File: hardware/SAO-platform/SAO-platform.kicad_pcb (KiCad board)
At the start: 2 copper layers, 85 parts, among them U1 WCH CH32V003F4U6

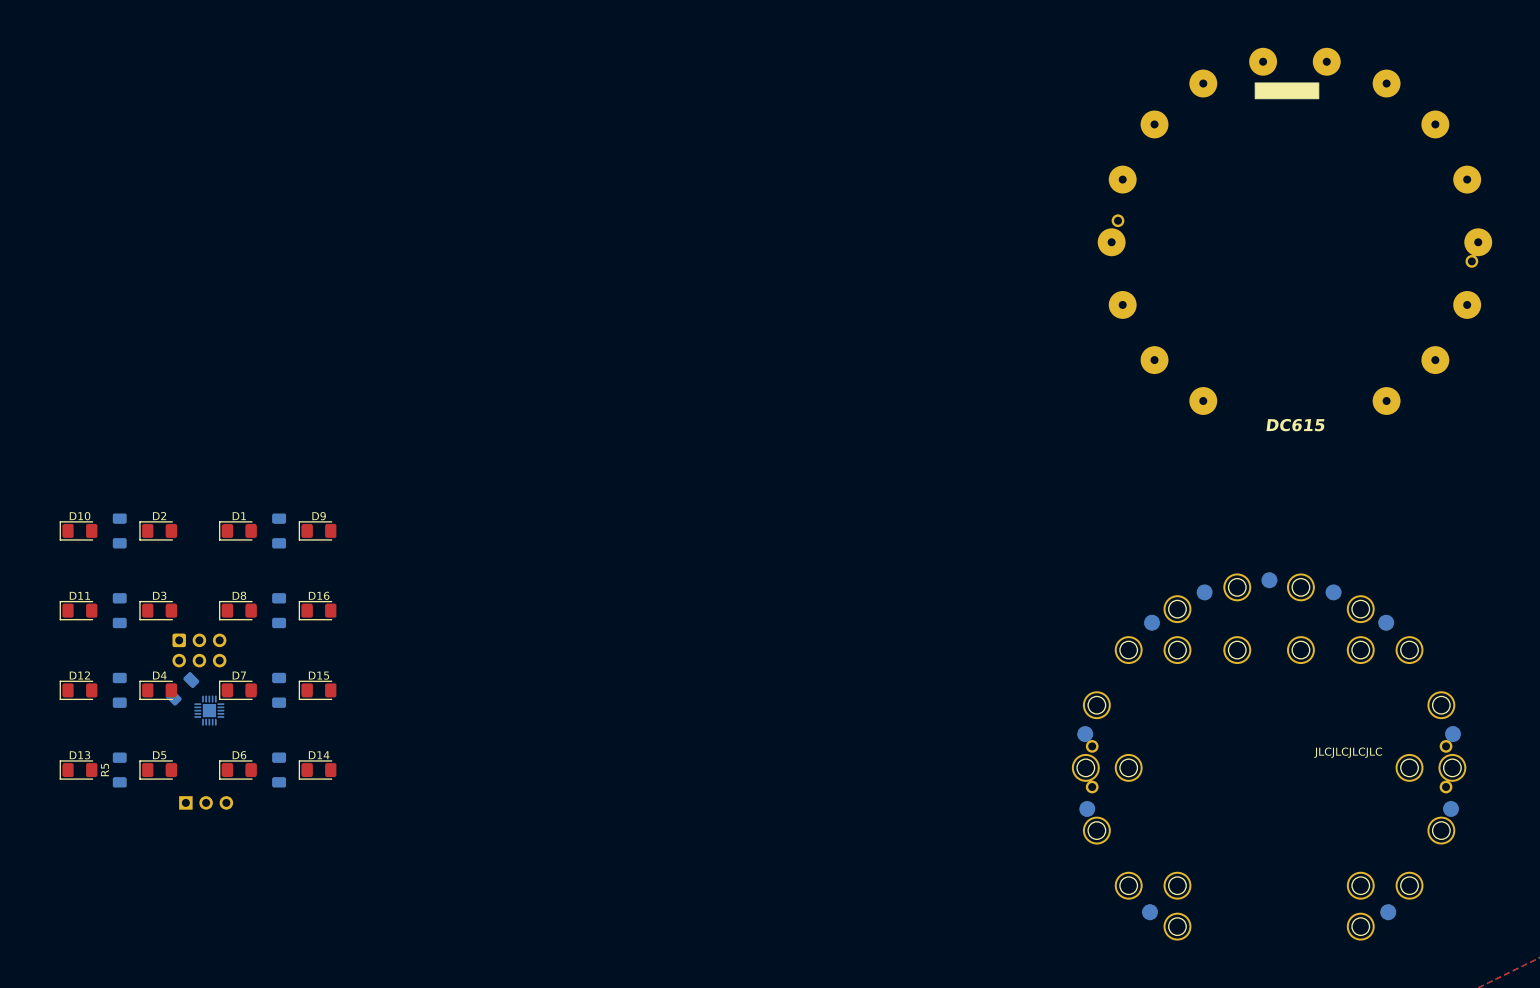
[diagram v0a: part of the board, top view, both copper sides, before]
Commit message: layout complete, passes DRC
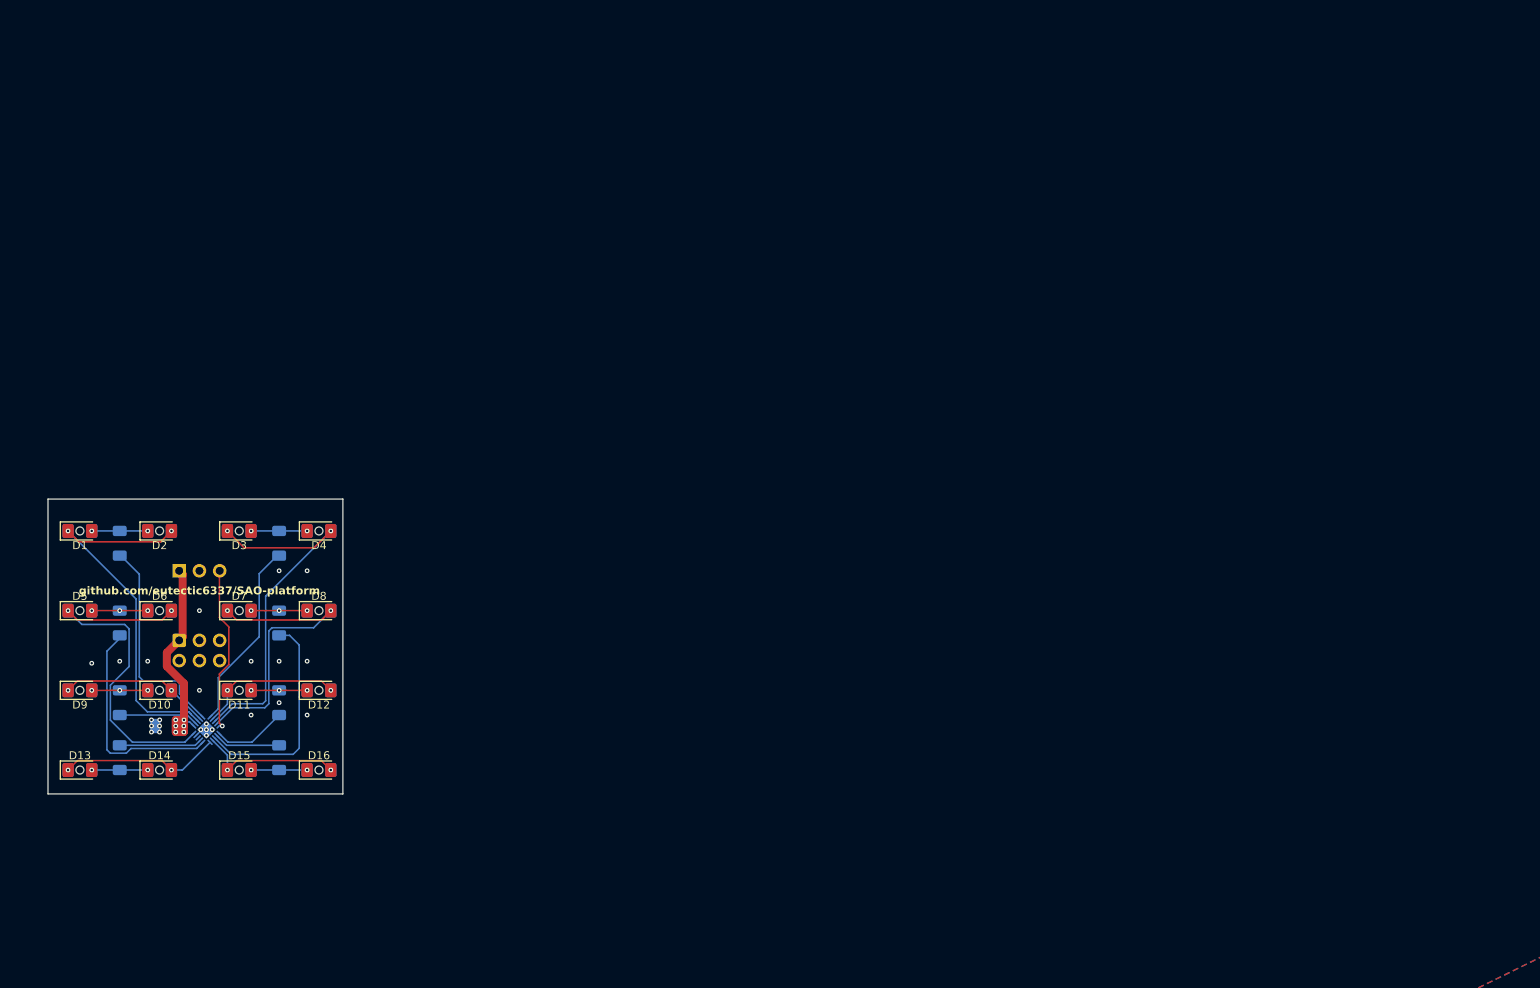
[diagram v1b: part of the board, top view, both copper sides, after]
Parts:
- removed align-io1, align-io2, align-ir1, align-ir2, align-o1, align-o2: , 
- removed aperture-D1, aperture-D10, aperture-D11, aperture-D12, aperture-D13, aperture-D14, aperture-D15, aperture-D16, aperture-D2, aperture-D3, aperture-D4, aperture-D5, aperture-D6, aperture-D7, aperture-D8, aperture-D9: TestPoint_THTPad_D1.0mm_Drill0.5mm, TestPoint:TestPoint_THTPad_D1.0mm_Drill0.5mm
- removed clearance-D1, clearance-D10, clearance-D11, clearance-D12, clearance-D13, clearance-D14, clearance-D15, clearance-D16, clearance-D2, clearance-D3, clearance-D4, clearance-D5, clearance-D6, clearance-D7, clearance-D8, clearance-D9, clearance-R1, clearance-R2, clearance-R3, clearance-R4, clearance-R5, clearance-R6, clearance-R7, clearance-R8: TestPoint_THTPad_3.0x3.0mm_Drill1.5mm, TestPoint:TestPoint_THTPad_3.0x3.0mm_Drill1.5mm
- removed stitch2 (x11): TestPoint_Pad_D2.0mm, TestPoint:TestPoint_Pad_D2.0mm
- added h1: , , F.Cu at (105.0, 85.0)
- added h10: , , F.Cu at (85.0, 85.0)
- added h11: , , F.Cu at (85.0, 95.0)
- added h12: , , F.Cu at (85.0, 105.0)
- added h13: , , F.Cu at (85.0, 115.0)
- added h14: , , F.Cu at (115.0, 115.0)
- added h15: , , F.Cu at (115.0, 105.0)
- added h16: , , F.Cu at (115.0, 95.0)
- added h2: , , F.Cu at (95.0, 85.0)
- added h3: , , F.Cu at (95.0, 95.0)
- added h4: , , F.Cu at (95.0, 105.0)
- added h5: , , F.Cu at (95.0, 115.0)
- added h6: , , F.Cu at (105.0, 115.0)
- added h7: , , F.Cu at (105.0, 105.0)
- added h8: , , F.Cu at (105.0, 95.0)
- added h9: , , F.Cu at (115.0, 85.0)
- added rD1: LED, LED_SMD:LED_1206_3216Metric_Pad1.42x1.75mm_HandSolder, B.Cu at (85.0, 85.0)
- added rD10: LED, LED_SMD:LED_1206_3216Metric_Pad1.42x1.75mm_HandSolder, B.Cu at (95.0, 105.0)
- added rD11: LED, LED_SMD:LED_1206_3216Metric_Pad1.42x1.75mm_HandSolder, B.Cu at (105.0, 105.0)
- added rD12: LED, LED_SMD:LED_1206_3216Metric_Pad1.42x1.75mm_HandSolder, B.Cu at (115.0, 105.0)
- added rD13: LED, LED_SMD:LED_1206_3216Metric_Pad1.42x1.75mm_HandSolder, B.Cu at (85.0, 115.0)
- added rD14: LED, LED_SMD:LED_1206_3216Metric_Pad1.42x1.75mm_HandSolder, B.Cu at (95.0, 115.0)
- added rD15: LED, LED_SMD:LED_1206_3216Metric_Pad1.42x1.75mm_HandSolder, B.Cu at (105.0, 115.0)
- added rD16: LED, LED_SMD:LED_1206_3216Metric_Pad1.42x1.75mm_HandSolder, B.Cu at (115.0, 115.0)
- added rD2: LED, LED_SMD:LED_1206_3216Metric_Pad1.42x1.75mm_HandSolder, B.Cu at (95.0, 85.0)
- added rD3: LED, LED_SMD:LED_1206_3216Metric_Pad1.42x1.75mm_HandSolder, B.Cu at (105.0, 85.0)
- added rD4: LED, LED_SMD:LED_1206_3216Metric_Pad1.42x1.75mm_HandSolder, B.Cu at (115.0, 85.0)
- added rD5: LED, LED_SMD:LED_1206_3216Metric_Pad1.42x1.75mm_HandSolder, B.Cu at (85.0, 95.0)
- added rD6: LED, LED_SMD:LED_1206_3216Metric_Pad1.42x1.75mm_HandSolder, B.Cu at (95.0, 95.0)
- added rD7: LED, LED_SMD:LED_1206_3216Metric_Pad1.42x1.75mm_HandSolder, B.Cu at (105.0, 95.0)
- added rD8: LED, LED_SMD:LED_1206_3216Metric_Pad1.42x1.75mm_HandSolder, B.Cu at (115.0, 95.0)
- added rD9: LED, LED_SMD:LED_1206_3216Metric_Pad1.42x1.75mm_HandSolder, B.Cu at (85.0, 105.0)
- moved PROG1 29.1 mm to (97.5, 90.0)
- moved C1 5.02 mm to (96.0, 109.5), turned to 180 degrees
- moved U1 2.42 mm to (100.9, 109.9), turned to 45 degrees
- moved R1 1.55 mm to (90.0, 86.6)
- moved R2 1.55 mm to (110.0, 86.6)
- moved R3 1.55 mm to (90.0, 96.6)
- moved R4 1.55 mm to (110.0, 96.6)
- moved R5 1.55 mm to (90.0, 106.6), turned to 90 degrees
- moved R6 1.55 mm to (110.0, 106.6), turned to 90 degrees
- moved R7 1.55 mm to (90.0, 113.4)
- moved R8 1.55 mm to (110.0, 113.4)
- renumbered D10 to D1, D4 to D10, D7 to D11, D15 to D12, D5 to D14, D6 to D15, D14 to D16, D1 to D3, D9 to D4, D11 to D5, D3 to D6, D8 to D7, D16 to D8, D12 to D9, R2 to R1, R1 to R2, R8 to R4, R4 to R5, R7 to R6, R5 to R7, R6 to R8
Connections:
- D1 pad 1: Net-(D10-K) -> GP1
- D1 pad 2: GP2 -> Net-(D1-A)
- D10 pad 1: GP4 -> Net-(D10-K)
- D10 pad 2: Net-(D12-K) -> GP5
- D11 pad 1: GP7 -> GP6
- D12 pad 2: GP7 -> GP6
- D13 pad 1: Net-(D13-K) -> GP7
- D13 pad 2: GP5 -> Net-(D13-A)
- D14 pad 1: GP5 -> Net-(D13-A)
- D14 pad 2: Net-(D13-K) -> GP7
- D15 pad 1: GP6 -> GP8
- D16 pad 2: GP6 -> GP8
- D2 pad 1: GP2 -> Net-(D1-A)
- D2 pad 2: Net-(D10-K) -> GP1
- D3 pad 1: GP1 -> GP2
- D4 pad 2: GP1 -> GP2
- D5 pad 1: Net-(D11-K) -> GP3
- D5 pad 2: GP3 -> Net-(D5-A)
- D6 pad 1: GP3 -> Net-(D5-A)
- D6 pad 2: Net-(D11-K) -> GP3
- D7 pad 1: GP8 -> GP4
- D8 pad 2: GP8 -> GP4
- D9 pad 1: Net-(D12-K) -> GP5
- D9 pad 2: GP4 -> Net-(D10-K)
- R1 pad 1: PWM2 -> PWM1
- R1 pad 2: Net-(D10-K) -> Net-(D1-A)
- R2 pad 1: PWM1 -> PWM2
- R3 pad 2: Net-(D11-K) -> Net-(D5-A)
- R4 pad 1: PWM8 -> PWM4
- R5 pad 1: PWM4 -> PWM5
- R5 pad 2: Net-(D12-K) -> Net-(D10-K)
- R6 pad 1: PWM7 -> PWM6
- R7 pad 1: PWM5 -> PWM7
- R7 pad 2: Net-(D13-K) -> Net-(D13-A)
- R8 pad 1: PWM6 -> PWM8
- U1 pad 1: PWM4 -> PWM3
- U1 pad 11: PWM8 -> PWM2
- U1 pad 12: GP8 -> GP6
- U1 pad 13: GP6 -> GP2
- U1 pad 14: GP7 -> GP4
- U1 pad 16: PWM7 -> PWM6
- U1 pad 17: PWM6 -> PWM8
- U1 pad 18: PWM5 -> PWM4
- U1 pad 19: GP5 -> GP8
- U1 pad 2: PWM3 -> PWM7
- U1 pad 20: GP4 -> GP7
- U1 pad 7: PWM2 -> PWM5
- U1 pad 8: GP2 -> GP1
- U1 pad 9: GP1 -> GP5
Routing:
- net GP1: track 0.00 -> 48.3 mm, vias 0 -> 2
- net GP3: track 0.00 -> 47.0 mm, vias 0 -> 2
- net GP2: track 0.00 -> 46.9 mm, vias 0 -> 2
- net GP4: track 0.00 -> 39.5 mm, vias 0 -> 2
- net +3V0: track 0.00 -> 28.1 mm, vias 0 -> 6
- net PWM4: track 0.00 -> 27.8 mm
- net PWM3: track 0.00 -> 27.8 mm
- net PWM1: track 0.00 -> 27.1 mm
- net PWM2: track 0.00 -> 24.0 mm
- net /SWIO: track 0.00 -> 20.6 mm, vias 0 -> 1
- net GP7: track 0.00 -> 20.2 mm, vias 0 -> 2
- net GP5: track 0.00 -> 19.1 mm, vias 0 -> 2
- net GP8: track 0.00 -> 18.5 mm, vias 0 -> 2
- net GP6: track 0.00 -> 18.4 mm, vias 0 -> 2
- net PWM7: track 0.00 -> 10.4 mm
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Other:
- board outline added: 37 x 37 mm
- board text added: "3V3"
- board text added: "SWD"
- board text removed: "JLCJLCJLCJLC"

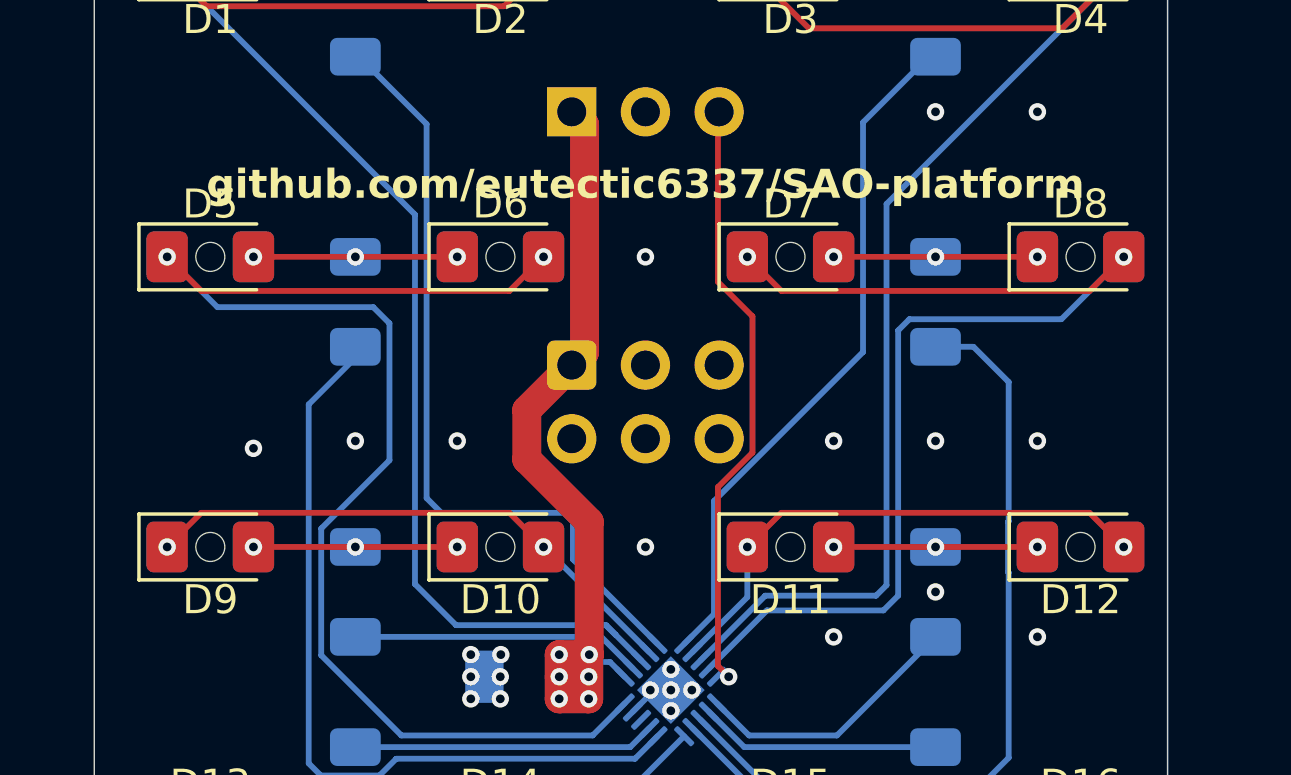
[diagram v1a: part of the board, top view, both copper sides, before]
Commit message: placed silk inc. repo QR; extended ground
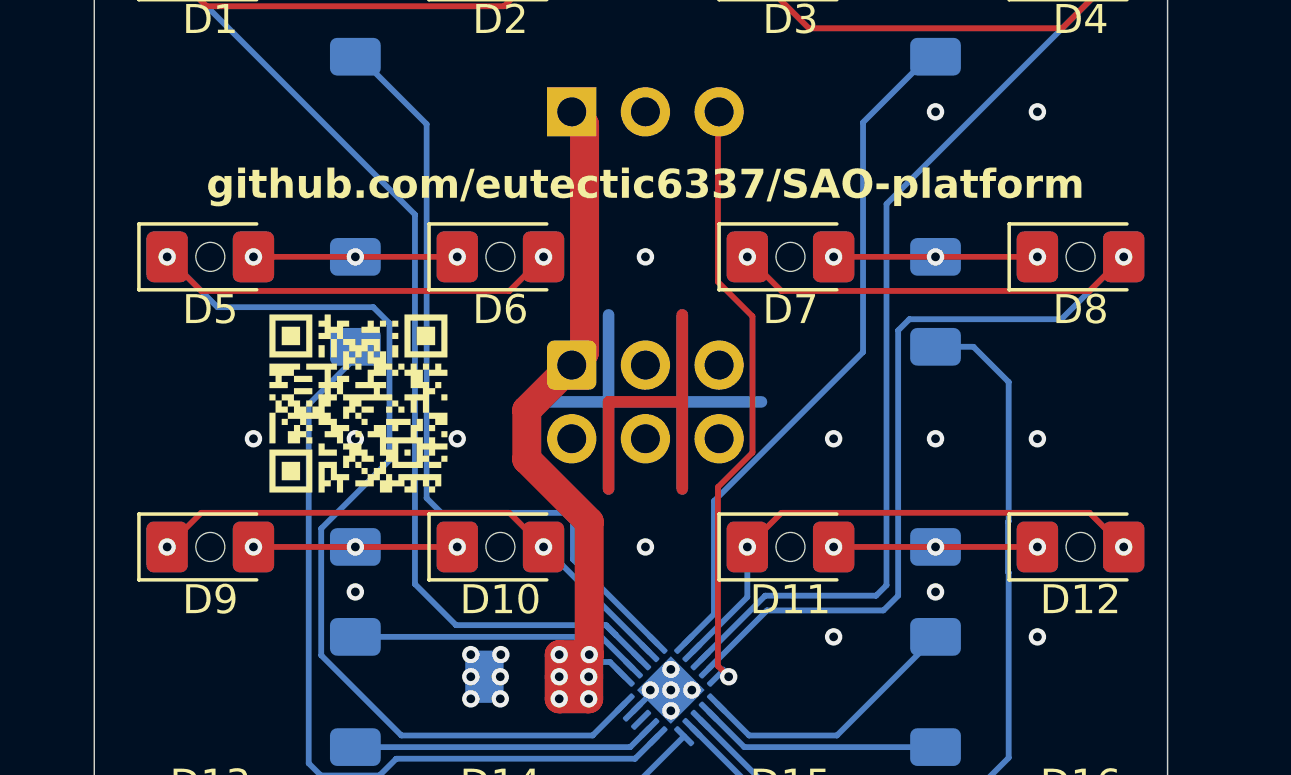
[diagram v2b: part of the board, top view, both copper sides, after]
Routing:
- net GND: vias 24 -> 25

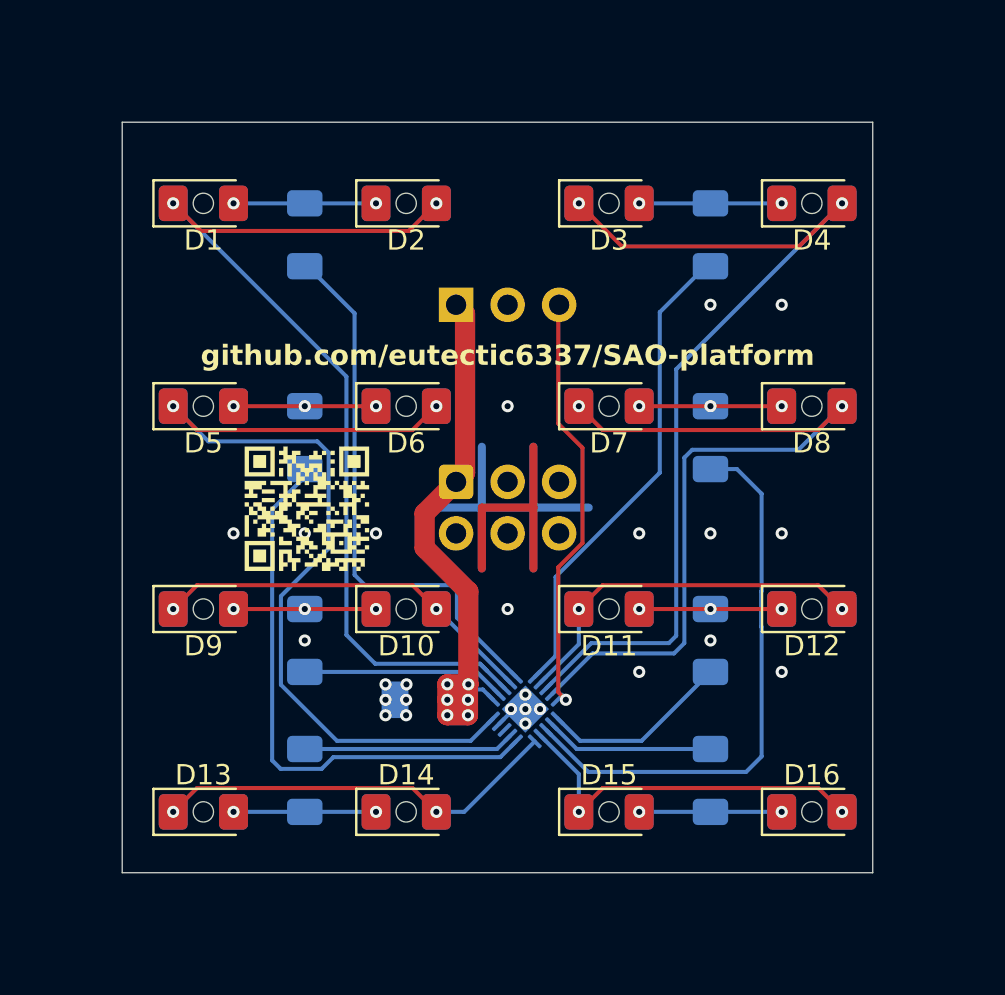
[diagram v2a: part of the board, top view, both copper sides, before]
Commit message: tweak edge cuts to make size "nice"
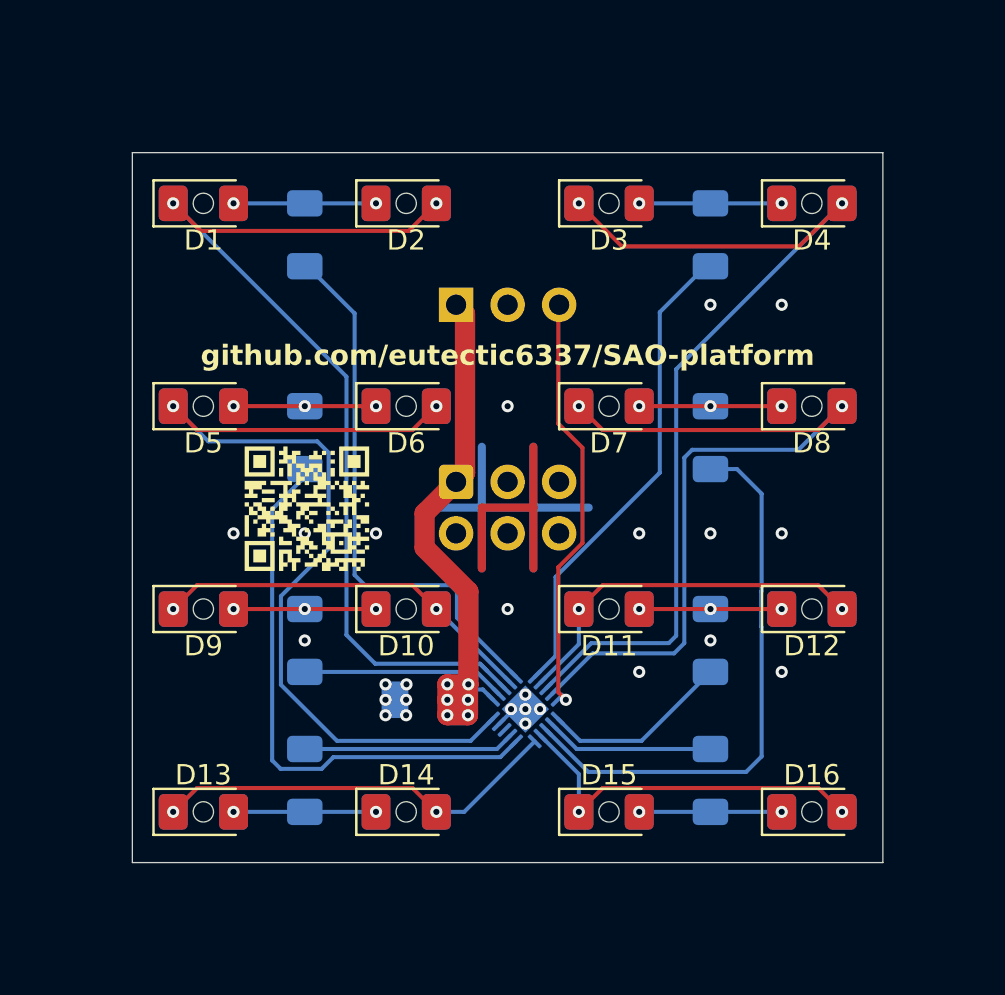
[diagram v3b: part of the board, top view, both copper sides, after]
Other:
- board size 37 x 37 mm -> 37 x 35 mm
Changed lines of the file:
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@@
 	)
 	(gr_rect
-		(start 81 81)
-		(end 118 118)
+		(start 81.5 82.5)
+		(end 118.5 117.5)
 		(stroke
 			(width 0.05)
